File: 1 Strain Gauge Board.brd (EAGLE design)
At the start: 160 x 100 mm, 39 parts, among them IC1 LM317MABDT, IC2 LM317MABDT, IC3 74LS674DW, J1 SD_CARD_SOCKET, Q1 16MHz, U1 LTC6082HGNPBF, U2 AD5254BRUZ1, U3 MAX11610EEE+, U4 ATMEGA328P_TQFP, U5 TXB0108DQSR

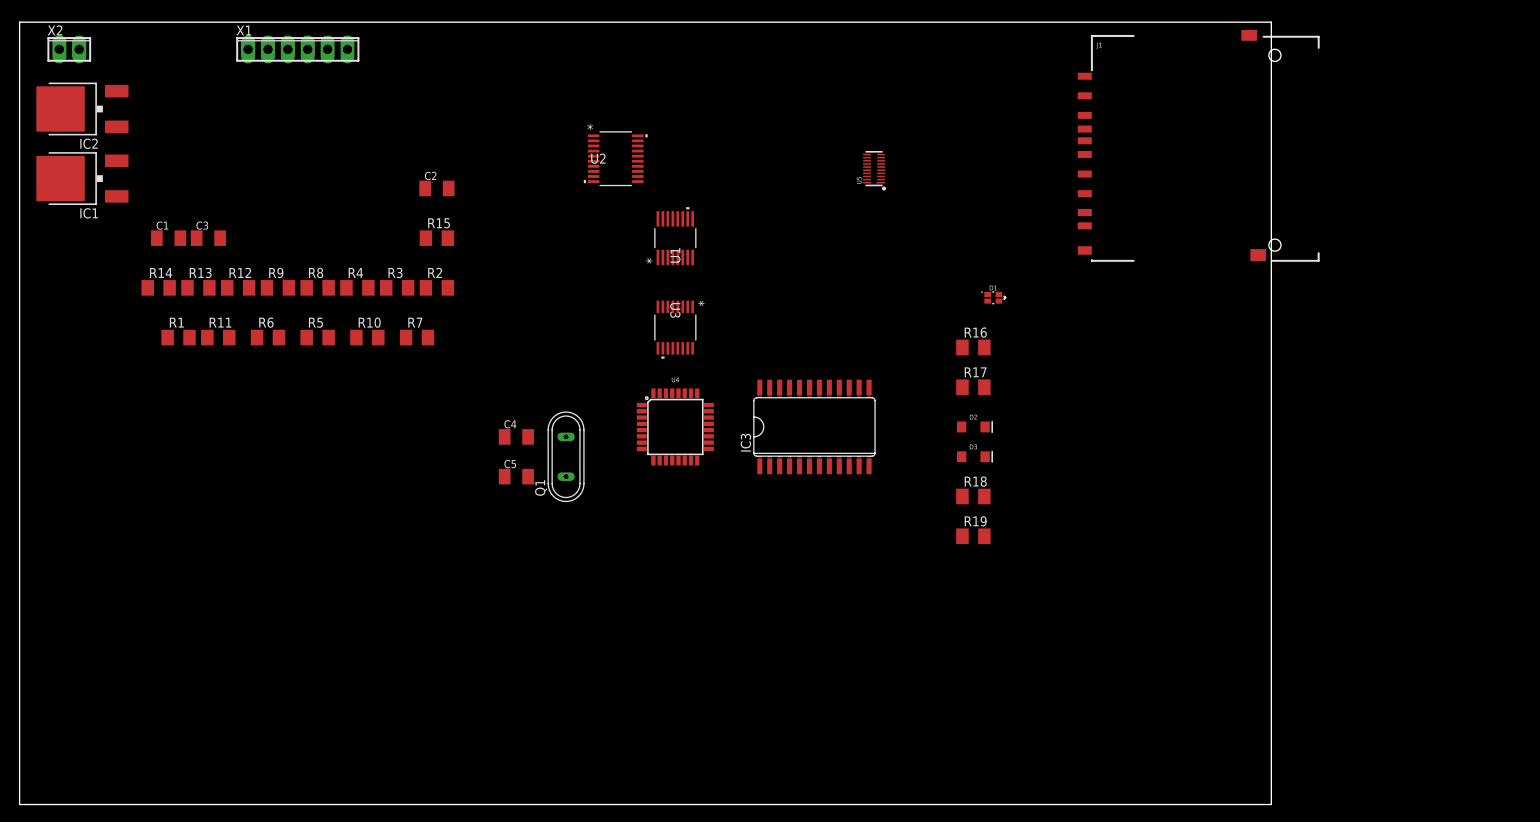
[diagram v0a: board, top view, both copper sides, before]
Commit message: Version 1 FINAL
Nearly complete version of the first iteration of the strain gauge logger.
TODO: Check SD card for validity. I have no idea how it's supposed to be hooked up.
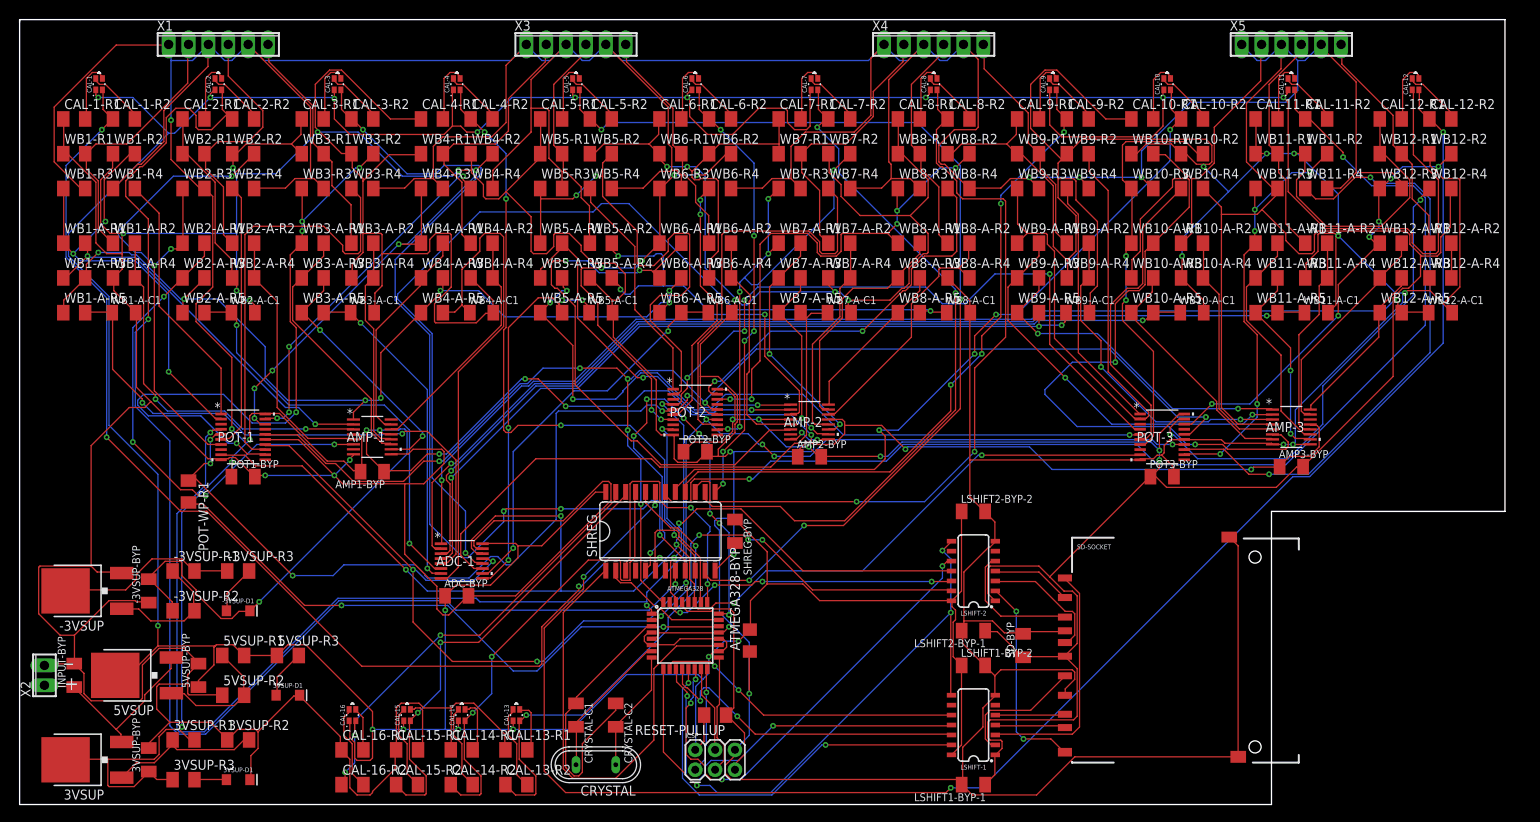
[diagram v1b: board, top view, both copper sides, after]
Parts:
- removed C1, C2: .1uF, resistor:C1206K
- removed C3: .01uF, resistor:C1206K
- removed C4, C5: 22pF, resistor:C1206K
- removed D1: LED-RGLTST-C195KGJRKT, SparkFun-LED:LTST-C195KGJRKT
- removed D2, D3: GREEN, SparkFun-LED:LED-1206
- removed IC1, IC2: LM317MABDT, v-reg:DPACK
- removed IC3: 74LS674DW, 74xx-eu:SO24W
- removed J1: SD_CARD_SOCKET, SparkFun-Connectors:SD
- removed Q1: 16MHz, special:QS
- removed R1, R2: 350, resistor:M1206
- removed R10: 100k, resistor:M1206
- removed R11, R5, R6: 10M, resistor:M1206
- removed R12, R14, R16, R17, R19: 330, resistor:M1206
- removed R13: 462, resistor:M1206
- removed R15: 990, resistor:M1206
- removed R18: 150, resistor:M1206
- removed R3: 370, resistor:M1206
- removed R4: 5k, resistor:M1206
- removed R7: 9.76M, resistor:M1206
- removed R8: 10K, resistor:M1206
- removed R9: 100, resistor:M1206
- removed U1: LTC6082HGNPBF, LTC6082 Strain Gauge Amplifier:SSOP-16_GN
- removed U2: AD5254BRUZ1, AD5254 4x1k Digital Potentiometer:RU_20
- removed U3: MAX11610EEE+, MAX11610 10 bit ADC:21-0055H_16
- removed U4: ATMEGA328P_TQFP, SparkFun-IC-Microcontroller:TQFP32-08
- removed U5: TXB0108DQSR, SparkFun-IC-Comms:UFDFN-20
- added -3VSUP, 3VSUP: LM317ABDT, v-reg:DPACK
- added -3VSUP-BYP, INPUT-BYP: .1uF, rcl:C1206K
- added -3VSUP-D1, 3VSUP-D1, 5VSUP-D1: GREEN, SparkFun-LED:LED-1206
- added -3VSUP-R1: 330, rcl:M1206
- added -3VSUP-R2: 462, rcl:M1206
- added -3VSUP-R3: 150, rcl:M1206
- added 3VSUP-BYP, 5VSUP-BYP: .1uF, resistor:C1206K
- added 3VSUP-R1, 5VSUP-R1, 5VSUP-R3, CAL-1-R1, CAL-1-R2, CAL-10-R1, CAL-10-R2, CAL-11-R1, CAL-11-R2, CAL-12-R1, CAL-12-R2, CAL-13-R1, CAL-13-R2, CAL-14-R1, CAL-14-R2, CAL-15-R1, CAL-15-R2, CAL-16-R1, CAL-16-R2, CAL-2-R1, CAL-2-R2, CAL-3-R1, CAL-3-R2, CAL-4-R1, CAL-4-R2, CAL-5-R1, CAL-5-R2, CAL-6-R1, CAL-6-R2, CAL-7-R1, CAL-7-R2, CAL-8-R1, CAL-8-R2, CAL-9-R1, CAL-9-R2: 330, resistor:M1206
- added 3VSUP-R2: 462, resistor:M1206
- added 3VSUP-R3: 150, resistor:M1206
- added 5VSUP: LM317MABDT, v-reg:DPACK
- added 5VSUP-R2: 990, resistor:M1206
- added ADC-1: MAX11610EEE+, MAX11610 10 bit ADC:21-0055H_16
- added ADC-BYP, LSHIFT1-BYP-1, LSHIFT1-BYP-2, LSHIFT2-BYP-1, LSHIFT2-BYP-2, POT1-BYP, POT2-BYP, POT3-BYP, SD-BYP, SHREG-BYP: .01uF, resistor:C1206K
- added AMP-1, AMP-2, AMP-3: LTC6082HGNPBFSSOP-16_GN-L, LTC6082 Strain Gauge Amplifier:SSOP-16_GN-L
- added AMP1-BYP, AMP2-BYP, AMP3-BYP: .01uF, rcl:C1206K
- added ATMEGA328: (no value), SparkFun-IC-Microcontroller:TQFP32-08
- added ATMEGA328-BYP: (no value), rcl:C1206
- added CAL-1, CAL-10, CAL-11, CAL-12, CAL-13, CAL-14, CAL-15, CAL-16, CAL-2, CAL-3, CAL-4, CAL-5, CAL-6, CAL-7, CAL-8, CAL-9: LED-RGLTST-C195KGJRKT, SparkFun-LED:LTST-C195KGJRKT
- added CRYSTAL: 16MHz, special:QS
- added CRYSTAL-C1, CRYSTAL-C2: 22pF, resistor:C1206K
- added ICSP: (no value), SparkFun-Connectors:2X3
- added LSHIFT-1, LSHIFT-2: TXB0104, SparkFun-IC-Comms:SO14
- added POT-1, POT-2, POT-3: AD5254BRUZ1, AD5254 4x1k Digital Potentiometer:RU_20
- added POT-WP-R1: 100, rcl:M1206
- added RESET-PULLUP: 10k, rcl:M1206
- added SD-SOCKET: SD_CARD_SOCKET, SparkFun-Connectors:SD
- added SHREG: 74LS674DW, 74xx-eu:SO24W
- added WB1-A-C1, WB10-A-C1, WB11-A-C1, WB12-A-C1, WB2-A-C1, WB3-A-C1, WB4-A-C1, WB5-A-C1, WB6-A-C1, WB7-A-C1, WB8-A-C1, WB9-A-C1: 100nF, rcl:C1206K
- added WB1-A-R1, WB1-A-R2, WB10-A-R1, WB10-A-R2, WB11-A-R1, WB11-A-R2, WB12-A-R1, WB12-A-R2, WB2-A-R1, WB2-A-R2, WB3-A-R1, WB3-A-R2, WB4-A-R1, WB4-A-R2, WB5-A-R1, WB5-A-R2, WB6-A-R1, WB6-A-R2, WB7-A-R1, WB7-A-R2, WB8-A-R1, WB8-A-R2, WB9-A-R1, WB9-A-R2: 1k, rcl:M1206
- added WB1-A-R3, WB1-A-R4, WB10-A-R3, WB10-A-R4, WB11-A-R3, WB11-A-R4, WB12-A-R3, WB12-A-R4, WB2-A-R3, WB2-A-R4, WB3-A-R3, WB3-A-R4, WB4-A-R3, WB4-A-R4, WB5-A-R3, WB5-A-R4, WB6-A-R3, WB6-A-R4, WB7-A-R3, WB7-A-R4, WB8-A-R3, WB8-A-R4, WB9-A-R3, WB9-A-R4: 1M, rcl:M1206
- added WB1-A-R5, WB10-A-R5, WB11-A-R5, WB12-A-R5, WB2-A-R5, WB3-A-R5, WB4-A-R5, WB5-A-R5, WB6-A-R5, WB7-A-R5, WB8-A-R5, WB9-A-R5: 100k, rcl:M1206
- added WB1-R1, WB1-R2: 350, resistor:M1206
- added WB1-R3: 370, resistor:M1206
- added WB1-R4: 5k, resistor:M1206
- added WB10-R1, WB10-R2, WB11-R1, WB11-R2, WB12-R1, WB12-R2, WB2-R1, WB2-R2, WB3-R1, WB3-R2, WB4-R1, WB4-R2, WB5-R1, WB5-R2, WB6-R1, WB6-R2, WB7-R1, WB7-R2, WB8-R1, WB8-R2, WB9-R1, WB9-R2: 350, rcl:M1206
- added WB10-R3, WB11-R3, WB12-R3, WB2-R3, WB3-R3, WB4-R3, WB5-R3, WB6-R3, WB7-R3, WB8-R3, WB9-R3: 370, rcl:M1206
- added WB10-R4, WB11-R4, WB12-R4, WB2-R4, WB3-R4, WB4-R4, WB5-R4, WB6-R4, WB7-R4, WB8-R4, WB9-R4: 5k, rcl:M1206
- added X3, X4, X5: (no value), con-phoenix-254:6POL254
- moved X2 80.1 mm to (3.17, 16.5), turned to 90 degrees
- moved X1 10.2 mm to (25.4, 97.2)
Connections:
- removed net +3V3: C1.2, IC1.4, J1.4, R12.2, R18.1, R3.2, R4.1, R8.2, U1.4, U5.5, X1.1, X1.4, X1.6
- removed net N$10: U3.14, U4.27
- removed net N$11: U3.13, U4.28
- removed net N$16: U4.9, U5.6
- removed net N$3: R11.1, R6.2, U1.2
- removed net N$4: R11.2, U1.1, U1.5
- removed net N$6: R5.2, R7.1, U1.3
- removed net N$7: C2.1, R7.2, R8.1, R9.1
- removed net N$8: C3.2, R10.1, R9.2, U1.6
- removed net N$9: C3.1, R10.2, U1.7, U3.5
- removed net VDD: U2.20
- removed net VSS: U2.10
- new net +3V: 3VSUP-BYP.1, 3VSUP-R1.2, 3VSUP-R3.1, 3VSUP.4, AMP-1.4, AMP-2.4, AMP-3.4, AMP1-BYP.2, AMP2-BYP.2, AMP3-BYP.2, LSHIFT-1.1, LSHIFT-2.1, LSHIFT1-BYP-1.1, LSHIFT2-BYP-1.1, POT-1.20, POT-2.20, POT-3.20, POT1-BYP.1, POT2-BYP.1, POT3-BYP.1, SD-BYP.1, SD-SOCKET.4, WB1-R3.2, WB1-R4.1, WB10-R3.2, WB10-R4.2, WB11-R3.2, WB11-R4.2, WB12-R3.2, WB12-R4.2, WB2-R3.2, WB2-R4.2, WB3-R3.2, WB3-R4.2, WB4-R3.2, WB4-R4.2, WB5-R3.2, WB5-R4.2, WB6-R3.2, WB6-R4.2, WB7-R3.2, WB7-R4.2, WB8-R3.2, WB8-R4.2, WB9-R3.2, WB9-R4.2, X1.1, X1.3, X1.5, X3.1, X3.3, X3.5, X4.1, X4.3, X4.5, X5.1, X5.3, X5.5
- new net -3V: -3VSUP-R1.2, -3VSUP-R3.1, -3VSUP.4
- new net LSHIFT-OE: ATMEGA328.9, LSHIFT-1.8, LSHIFT-2.8
- new net MISO: ATMEGA328.16, ICSP.1
- new net MOSI: ATMEGA328.15, ICSP.4
- new net N$41: CAL-2-R1.2, CAL-2.P$4
- new net N$42: CAL-2-R2.2, CAL-2.P$3
- new net N$45: CAL-2-R2.1, CAL-2.P$2, SHREG.8
- new net N$46: CAL-5-R1.2, CAL-5.P$4
- new net N$47: CAL-5-R2.2, CAL-5.P$3
- new net N$48: CAL-5-R2.1, CAL-5.P$2, SHREG.11
- new net N$49: CAL-8-R1.2, CAL-8.P$4
- new net N$50: CAL-8-R2.2, CAL-8.P$3
- new net N$51: CAL-8-R2.1, CAL-8.P$2, SHREG.15
- new net N$52: CAL-6-R1.2, CAL-6.P$4
- new net N$53: CAL-6-R2.2, CAL-6.P$3
- new net N$54: CAL-6-R2.1, CAL-6.P$2, SHREG.13
- new net N$55: CAL-3-R1.2, CAL-3.P$4
- new net N$56: CAL-3-R2.2, CAL-3.P$3
- new net N$57: CAL-3-R2.1, CAL-3.P$2, SHREG.9
- new net N$58: CAL-9-R1.2, CAL-9.P$4
- new net N$59: CAL-9-R2.2, CAL-9.P$3
- new net N$60: CAL-9-R2.1, CAL-9.P$2, SHREG.16
- new net N$61: CAL-11-R1.2, CAL-11.P$4
- new net N$62: CAL-11-R2.2, CAL-11.P$3
- new net N$63: CAL-11-R2.1, CAL-11.P$2, SHREG.18
- new net N$64: CAL-12-R1.2, CAL-12.P$4
- new net N$65: CAL-12-R2.2, CAL-12.P$3
- new net N$66: CAL-12-R2.1, CAL-12.P$2, SHREG.19
- new net N$67: CAL-14-R1.2, CAL-14.P$4
- new net N$68: CAL-14-R2.2, CAL-14.P$3
- new net N$69: CAL-14-R2.1, CAL-14.P$2, SHREG.21
- new net N$70: CAL-15-R1.2, CAL-15.P$4
- new net N$71: CAL-15-R2.2, CAL-15.P$3
- new net N$72: CAL-15-R2.1, CAL-15.P$2, SHREG.22
- new net N$73: CAL-7-R1.2, CAL-7.P$4
- new net N$74: CAL-7-R2.2, CAL-7.P$3
- new net N$75: CAL-7-R2.1, CAL-7.P$2, SHREG.14
- new net N$76: CAL-10-R1.2, CAL-10.P$4
- new net N$77: CAL-10-R2.2, CAL-10.P$3
- new net N$78: CAL-10-R2.1, CAL-10.P$2, SHREG.17
- new net N$79: CAL-13-R1.2, CAL-13.P$4
- new net N$80: CAL-13-R2.2, CAL-13.P$3
- new net N$81: CAL-13-R2.1, CAL-13.P$2, SHREG.20
- new net N$82: CAL-16-R1.2, CAL-16.P$4
- new net N$83: CAL-16-R2.2, CAL-16.P$3
- new net N$84: CAL-16-R2.1, CAL-16.P$2, SHREG.23
- new net N$85: CAL-4-R1.2, CAL-4.P$4
- new net N$86: CAL-4-R2.2, CAL-4.P$3
- new net N$87: CAL-4-R2.1, CAL-4.P$2, SHREG.10
- new net POT-SELECT-AD0: ATMEGA328.1, POT-1.4, POT-2.4, POT-3.4
- new net POT-SELECT-AD1: ATMEGA328.32, POT-1.16, POT-2.16, POT-3.16
- new net POT-WP: POT-1.5, POT-2.5, POT-3.5, POT-WP-R1.1
- new net RESET: ATMEGA328.29, ICSP.5, RESET-PULLUP.1
- new net SCK: ATMEGA328.17, ICSP.3
- new net SCL: ADC-1.13, ATMEGA328.28, POT-1.14, POT-2.14, POT-3.14
- new net SDA: ADC-1.14, ATMEGA328.27, POT-1.9, POT-2.9, POT-3.9
- new net SG1-AIN: ADC-1.5, WB1-A-C1.1, WB1-A-R5.2
- new net SG1-NEG: WB1-A-R2.1, WB1-R1.2, X1.2
- new net SG1-POS: POT-1.2, WB1-A-R1.1, WB1-R2.2, WB1-R3.1
- new net SG1-POT: POT-1.1, WB1-R4.2
- new net SG10-AIN: ADC-1.3, WB10-A-C1.1, WB10-A-R5.2
- new net SG10-NEG: WB10-A-R2.1, WB10-R1.2, X5.2
- new net SG10-POS: POT-3.7, WB10-A-R1.1, WB10-R2.2, WB10-R3.1
- new net SG10-POT: POT-3.6, WB10-R4.1
- new net SG11-AIN: ADC-1.2, WB11-A-C1.1, WB11-A-R5.2
- new net SG11-NEG: WB11-A-R2.1, WB11-R1.2, X5.4
- new net SG11-POS: POT-3.12, WB11-A-R1.1, WB11-R2.2, WB11-R3.1
- new net SG11-POT: POT-3.13, WB11-R4.1
- new net SG12-AIN: ADC-1.1, WB12-A-C1.1, WB12-A-R5.2
- new net SG12-NEG: WB12-A-R2.1, WB12-R1.2, X5.6
- new net SG12-POS: POT-3.18, WB12-A-R1.1, WB12-R2.2, WB12-R3.1
- new net SG12-POT: POT-3.19, WB12-R4.1
- new net SG2-AIN: ADC-1.6, WB2-A-C1.1, WB2-A-R5.2
- new net SG2-NEG: WB2-A-R2.1, WB2-R1.2, X1.4
- new net SG2-POS: POT-1.7, WB2-A-R1.1, WB2-R2.2, WB2-R3.1
- new net SG2-POT: POT-1.6, WB2-R4.1
- new net SG3-AIN: ADC-1.7, WB3-A-C1.1, WB3-A-R5.2
- new net SG3-NEG: WB3-A-R2.1, WB3-R1.2, X1.6
- new net SG3-POS: POT-1.12, WB3-A-R1.1, WB3-R2.2, WB3-R3.1
- new net SG3-POT: POT-1.13, WB3-R4.1
- new net SG4-AIN: ADC-1.8, WB4-A-C1.1, WB4-A-R5.2
- new net SG4-NEG: WB4-A-R2.1, WB4-R1.2, X3.2
- new net SG4-POS: POT-1.18, WB4-A-R1.1, WB4-R2.2, WB4-R3.1
- new net SG4-POT: POT-1.19, WB4-R4.1
- new net SG5-AIN: ADC-1.9, WB5-A-C1.1, WB5-A-R5.2
- new net SG5-NEG: WB5-A-R2.1, WB5-R1.2, X3.4
- new net SG5-POS: POT-2.2, WB5-A-R1.1, WB5-R2.2, WB5-R3.1
- new net SG5-POT: POT-2.1, WB5-R4.1
- new net SG6-AIN: ADC-1.10, WB6-A-C1.1, WB6-A-R5.2
- new net SG6-NEG: WB6-A-R2.1, WB6-R1.2, X3.6
- new net SG6-POS: POT-2.7, WB6-A-R1.1, WB6-R2.2, WB6-R3.1
- new net SG6-POT: POT-2.6, WB6-R4.1
- new net SG7-AIN: ADC-1.11, WB7-A-C1.1, WB7-A-R5.2
- new net SG7-NEG: WB7-A-R2.1, WB7-R1.2, X4.2
- new net SG7-POS: POT-2.12, WB7-A-R1.1, WB7-R2.2, WB7-R3.1
- new net SG7-POT: POT-2.13, WB7-R4.1
- new net SG8-AIN: ADC-1.12, WB8-A-C1.1, WB8-A-R5.2
- new net SG8-NEG: WB8-A-R2.1, WB8-R1.2, X4.4
- new net SG8-POS: POT-2.18, WB8-A-R1.1, WB8-R2.2, WB8-R3.1
- new net SG8-POT: POT-2.19, WB8-R4.1
- new net SG9-AIN: ADC-1.4, WB9-A-C1.1, WB9-A-R5.2
- new net SG9-NEG: WB9-A-R2.1, WB9-R1.2, X4.6
- new net SG9-POS: POT-3.2, WB9-A-R1.1, WB9-R2.2, WB9-R3.1
- new net SG9-POT: POT-3.1, WB9-R4.1
- new net V-: -3VSUP-BYP.2, -3VSUP-D1.C, -3VSUP-R2.1, AMP-1.13, AMP-2.13, AMP-3.13, AMP1-BYP.1, AMP2-BYP.1, AMP3-BYP.1
- new net WB1-A-NEG: AMP-1.2, WB1-A-R1.2, WB1-A-R3.1
- new net WB1-A-OUT: AMP-1.1, WB1-A-R3.2, WB1-A-R5.1, WB2-A-R3.2, WB2-A-R5.1, WB4-A-R3.2, WB4-A-R5.1, WB6-A-R3.2, WB6-A-R5.1
- new net WB1-A-POS: AMP-1.3, WB1-A-R2.2, WB1-A-R4.2
- new net WB10-A-NEG: AMP-3.6, WB10-A-R1.2, WB10-A-R3.1
- new net WB10-A-OUT: AMP-3.7, WB10-A-R3.2, WB10-A-R5.1
- new net WB10-A-POS: AMP-3.5, WB10-A-R2.2, WB10-A-R4.2
- new net WB11-A-NEG: AMP-3.11, WB11-A-R1.2, WB11-A-R3.1
- new net WB11-A-OUT: AMP-3.10, WB11-A-R3.2, WB11-A-R5.1
- new net WB11-A-POS: AMP-3.12, WB11-A-R2.2, WB11-A-R4.2
- new net WB12-A-NEG: AMP-3.15, WB12-A-R1.2, WB12-A-R3.1
- new net WB12-A-OUT: AMP-3.16, WB12-A-R3.2, WB12-A-R5.1
- new net WB12-A-POS: WB12-A-R2.2, WB12-A-R4.2
- new net WB124-A-POS: AMP-3.14
- new net WB2-A-NEG: AMP-1.6, WB2-A-R1.2, WB2-A-R3.1
- new net WB2-A-OUT: AMP-1.7
- new net WB2-A-POS: AMP-1.5, WB2-A-R2.2, WB2-A-R4.2
- new net WB3-A-NEG: AMP-1.11, WB3-A-R1.2, WB3-A-R3.1
- new net WB3-A-OUT: AMP-1.10, WB3-A-R3.2, WB3-A-R5.1
- new net WB3-A-POS: AMP-1.12, WB3-A-R2.2, WB3-A-R4.2
- new net WB4-A-NEG: AMP-1.15, WB4-A-R1.2, WB4-A-R3.1
- new net WB4-A-OUT: AMP-1.16
- new net WB4-A-POS: AMP-1.14, WB4-A-R2.2, WB4-A-R4.2
- new net WB5-A-NEG: AMP-2.2, WB5-A-R1.2, WB5-A-R3.1
- new net WB5-A-OUT: AMP-2.1, WB5-A-R3.2, WB5-A-R5.1
- new net WB5-A-POS: AMP-2.3, WB5-A-R2.2, WB5-A-R4.2
- new net WB6-A-NEG: AMP-2.6, WB6-A-R1.2, WB6-A-R3.1
- new net WB6-A-OUT: AMP-2.7
- new net WB6-A-POS: AMP-2.5, WB6-A-R2.2, WB6-A-R4.2
- new net WB7-A-NEG: AMP-2.11, WB7-A-R1.2, WB7-A-R3.1
- new net WB7-A-OUT: AMP-2.10, WB7-A-R3.2, WB7-A-R5.1
- new net WB7-A-POS: AMP-2.12, WB7-A-R2.2, WB7-A-R4.2
- new net WB8-A-NEG: AMP-2.15, WB8-A-R1.2, WB8-A-R3.1
- new net WB8-A-OUT: AMP-2.16, WB8-A-R3.2, WB8-A-R5.1
- new net WB8-A-POS: AMP-2.14, WB8-A-R2.2, WB8-A-R4.2
- new net WB9-A-NEG: AMP-3.2, WB9-A-R1.2, WB9-A-R3.1
- new net WB9-A-OUT: AMP-3.1, WB9-A-R3.2, WB9-A-R5.1
- new net WB9-A-POS: AMP-3.3, WB9-A-R2.2, WB9-A-R4.2
- net +5V: now also 5VSUP-BYP.1, 5VSUP-R1.2, 5VSUP-R3.1, 5VSUP.4, ADC-1.16, ADC-BYP.1, ATMEGA328-BYP.2, ATMEGA328.18, ATMEGA328.20, ATMEGA328.4, ATMEGA328.6, CAL-1.P$1, CAL-10.P$1, CAL-11.P$1, CAL-12.P$1, CAL-13.P$1, CAL-14.P$1, CAL-15.P$1, CAL-16.P$1, CAL-2.P$1, CAL-3.P$1, CAL-4.P$1, CAL-5.P$1, CAL-6.P$1, CAL-7.P$1, CAL-8.P$1, CAL-9.P$1, ICSP.2, LSHIFT-1.14, LSHIFT-2.14, LSHIFT1-BYP-2.1, LSHIFT2-BYP-2.1, RESET-PULLUP.2, SHREG-BYP.1, SHREG.24; no longer D1.P$1, IC2.4, IC3.24, R14.2, R19.1, U3.16, U4.18, U4.20, U4.29, U4.4, U4.6, U5.16
- net GND: now also -3VSUP-BYP.1, -3VSUP.3, 3VSUP-BYP.2, 3VSUP-D1.C, 3VSUP-R2.1, 5VSUP-BYP.2, 5VSUP-D1.C, 5VSUP-R2.1, ADC-1.15, ADC-BYP.2, AMP-1.8, AMP-1.9, AMP-2.8, AMP-2.9, AMP-3.8, AMP-3.9, ATMEGA328-BYP.1, ATMEGA328.21, ATMEGA328.3, ATMEGA328.5, CAL-1-R1.1, CAL-10-R1.1, CAL-11-R1.1, CAL-12-R1.1, CAL-13-R1.1, CAL-14-R1.1, CAL-15-R1.1, CAL-16-R1.1, CAL-2-R1.1, CAL-3-R1.1, CAL-4-R1.1, CAL-5-R1.1, CAL-6-R1.1, CAL-7-R1.1, CAL-8-R1.1, CAL-9-R1.1, CRYSTAL-C1.1, CRYSTAL-C2.1, ICSP.6, INPUT-BYP.2, LSHIFT-1.7, LSHIFT-2.7, LSHIFT1-BYP-1.2, LSHIFT1-BYP-2.2, LSHIFT2-BYP-1.2, LSHIFT2-BYP-2.2, POT-1.10, POT-1.15, POT-2.10, POT-2.15, POT-3.10, POT-3.15, POT1-BYP.2, POT2-BYP.2, POT3-BYP.2, SD-BYP.2, SD-SOCKET.3, SD-SOCKET.6, SD-SOCKET.SH@1, SD-SOCKET.SH@2, SHREG-BYP.2, SHREG.12, WB1-A-C1.2, WB1-A-R4.1, WB1-R1.1, WB1-R2.1, WB10-A-C1.2, WB10-A-R4.1, WB10-R1.1, WB10-R2.1, WB11-A-C1.2, WB11-A-R4.1, WB11-R1.1, WB11-R2.1, WB12-A-C1.2, WB12-A-R4.1, WB12-R1.1, WB12-R2.1, WB2-A-C1.2, WB2-A-R4.1, WB2-R1.1, WB2-R2.1, WB3-A-C1.2, WB3-A-R4.1, WB3-R1.1, WB3-R2.1, WB4-A-C1.2, WB4-A-R4.1, WB4-R1.1, WB4-R2.1, WB5-A-C1.2, WB5-A-R4.1, WB5-R1.1, WB5-R2.1, WB6-A-C1.2, WB6-A-R4.1, WB6-R1.1, WB6-R2.1, WB7-A-C1.2, WB7-A-R4.1, WB7-R1.1, WB7-R2.1, WB8-A-C1.2, WB8-A-R4.1, WB8-R1.1, WB8-R2.1, WB9-A-C1.2, WB9-A-R4.1, WB9-R1.1, WB9-R2.1; no longer C1.1, C2.2, C4.1, C5.1, D2.C, D3.C, IC3.12, J1.3, J1.6, J1.SH@1, J1.SH@2, R1.1, R13.1, R15.1, R16.1, R2.1, U1.13, U3.15, U4.21, U4.3, U4.5, U5.15
- net N$1: now also -3VSUP-D1.A, -3VSUP-R3.2; no longer R2.2, R3.1, R5.1, U2.2
- net N$12: now also 3VSUP-R1.1, 3VSUP-R2.2, 3VSUP.1; no longer IC1.1, R12.1, R13.2
- net N$13: now also LSHIFT-2.4, SD-SOCKET.1; no longer J1.1, U5.3
- net N$14: now also 5VSUP-R1.1, 5VSUP-R2.2, 5VSUP.1; no longer IC2.1, R14.1, R15.2
- net N$15: now also LSHIFT-2.2, SD-SOCKET.WP; no longer J1.WP, U5.1
- net N$17: now also LSHIFT-2.3, SD-SOCKET.CD; no longer J1.CD, U5.2
- net N$18: now also LSHIFT-2.5, SD-SOCKET.2; no longer J1.2, U5.4
- net N$19: now also ATMEGA328.7, CRYSTAL-C1.2, CRYSTAL.2; no longer C4.2, Q1.2, U4.7
- net N$2: now also -3VSUP-R1.1, -3VSUP-R2.2, -3VSUP.1; no longer R1.2, R6.1, X1.2
- net N$20: now also ATMEGA328.8, CRYSTAL-C2.2, CRYSTAL.1; no longer C5.2, Q1.1, U4.8
- net N$21: now also LSHIFT-1.2, SD-SOCKET.5; no longer J1.5, U5.7
- net N$22: now also LSHIFT-1.3, SD-SOCKET.9; no longer J1.9, U5.8
- net N$23: now also LSHIFT-1.4, SD-SOCKET.8; no longer J1.8, U5.9
- net N$24: now also LSHIFT-1.5, SD-SOCKET.7; no longer J1.7, U5.10
- net N$25: now also CAL-1-R1.2, CAL-1.P$4; no longer D1.P$4, R16.2
- net N$26: now also CAL-1-R2.2, CAL-1.P$3; no longer D1.P$3, R17.2
- net N$27: now also CAL-1-R2.1, CAL-1.P$2, SHREG.7; no longer D1.P$2, IC3.7, R17.1
- net N$28: now also ATMEGA328.2, LSHIFT-2.13; no longer U4.17, U5.20
- net N$29: now also ATMEGA328.31, LSHIFT-2.12; no longer U4.16, U5.19
- net N$30: now also ATMEGA328.30, LSHIFT-2.11; no longer U4.15, U5.18
- net N$31: now also ATMEGA328.14, LSHIFT-2.10; no longer U4.14, U5.17
- net N$32: now also ATMEGA328.13, LSHIFT-1.13; no longer U4.13, U5.14
- net N$33: now also ATMEGA328.12, LSHIFT-1.12; no longer U4.12, U5.13
- net N$34: now also ATMEGA328.11, LSHIFT-1.11; no longer U4.11, U5.12
- net N$35: now also ATMEGA328.10, LSHIFT-1.10; no longer U4.10, U5.11
- net N$36: now also ATMEGA328.26, SHREG.6; no longer IC3.6, U4.26
- net N$37: now also ATMEGA328.23, SHREG.2; no longer IC3.2, U4.23
- net N$38: now also ATMEGA328.24, SHREG.5; no longer IC3.5, U4.24
- net N$39: now also ATMEGA328.25, SHREG.3; no longer IC3.3, U4.25
- net N$40: now also ATMEGA328.19, SHREG.1; no longer IC3.1, U4.19
- net N$43: now also 3VSUP-D1.A, 3VSUP-R3.2; no longer D3.A, R18.2
- net N$44: now also 5VSUP-D1.A, 5VSUP-R3.2; no longer D2.A, R19.2
- net N$5: now also ATMEGA328.22, POT-WP-R1.2; no longer R4.2, U2.1
- net VCC: now also 3VSUP.3, 5VSUP.3, INPUT-BYP.1; no longer IC1.3, IC2.3
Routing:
- net GND: track 0.00 -> 1556.2 mm, vias 0 -> 28
- net +3V: track 0.00 -> 987.2 mm, vias 0 -> 14
- net +5V: track 0.00 -> 630.8 mm, vias 0 -> 17
- net POT-SELECT-AD0: track 0.00 -> 225.9 mm, vias 0 -> 7
- net N$66: track 0.00 -> 215.2 mm, vias 0 -> 4
- net V-: track 0.00 -> 213.6 mm, vias 0 -> 9
- net SDA: track 0.00 -> 184.6 mm, vias 0 -> 6
- net SCL: track 0.00 -> 176.9 mm, vias 0 -> 8
- net N$45: track 0.00 -> 175.8 mm, vias 0 -> 2
- net POT-SELECT-AD1: track 0.00 -> 174.2 mm, vias 0 -> 7
- net POT-WP: track 0.00 -> 160.2 mm, vias 0 -> 6
- net N$63: track 0.00 -> 151.2 mm, vias 0 -> 2
- net SG12-AIN: track 0.00 -> 146.3 mm, vias 0 -> 2
- net N$27: track 0.00 -> 143.2 mm, vias 0 -> 4
- net SG11-AIN: track 0.00 -> 129.9 mm, vias 0 -> 2
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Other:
- board size 160 x 100 mm -> 189.9 x 100.3 mm
- board text added: "+"
- board text added: "_"
